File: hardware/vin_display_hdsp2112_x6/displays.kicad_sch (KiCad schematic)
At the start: 13 parts

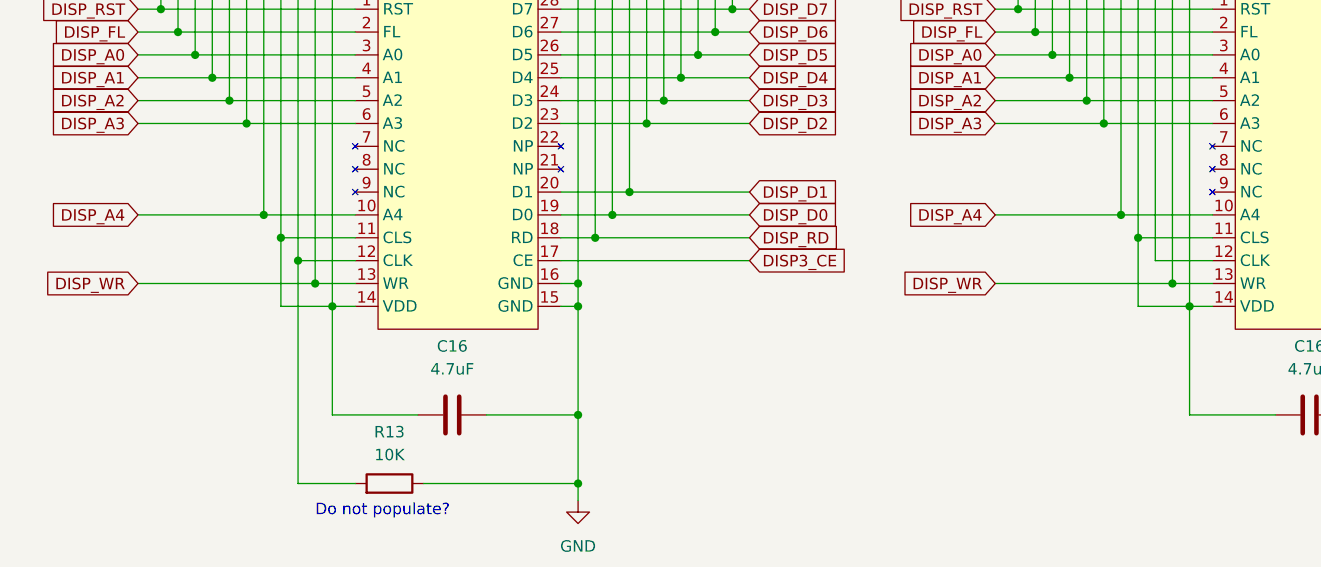
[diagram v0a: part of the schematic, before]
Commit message: work on hdsp2112_x6 pcb
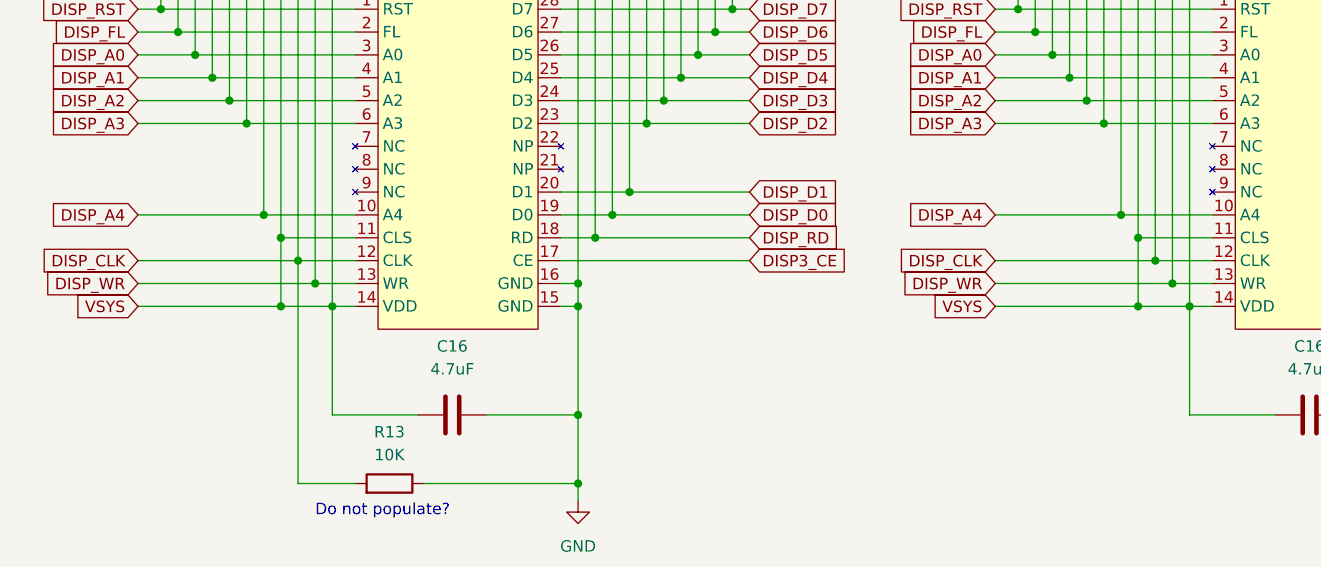
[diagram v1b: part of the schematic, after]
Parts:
- C16: footprint Capacitor_SMD:C_0603_1608Metric -> Capacitor_SMD:C_0805_2012Metric
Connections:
- net VSYS: now reaches C16.1, C16.1, C16.1, U10.11 (CLS), U10.14 (VDD), U8.11 (CLS), U8.14 (VDD), U9.11 (CLS), U9.14 (VDD)
- net VSYS: now also C16.1, C16.1, C16.1, U5.11 (CLS), U5.14 (VDD), U6.11 (CLS), U6.14 (VDD), U7.11 (CLS), U7.14 (VDD)
- net DISP_CLK: now reaches U10.12 (CLK), U8.12 (CLK), U9.12 (CLK)
- net DISP_CLK: now also R13.2, U5.12 (CLK), U6.12 (CLK), U7.12 (CLK)
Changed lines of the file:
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@@
   (junction (at 50.8 66.04) (diameter 0) (color 0 0 0 0)
   )
+  (junction (at 142.24 160.02) (diameter 0) (color 0 0 0 0)
+  )
   (junction (at 138.43 154.94) (diameter 0) (color 0 0 0 0)
   )
@@
   (junction (at 132.715 83.82) (diameter 0) (color 0 0 0 0)
   )
+  (junction (at 45.085 165.1) (diameter 0) (color 0 0 0 0)
+  )
   (junction (at 31.75 76.2) (diameter 0) (color 0 0 0 0)
   )
@@
   (junction (at 80.01 157.48) (diameter 0) (color 0 0 0 0)
   )
+  (junction (at 140.335 165.1) (diameter 0) (color 0 0 0 0)
+  )
   (junction (at 146.05 165.1) (diameter 0) (color 0 0 0 0)
   )
@@
     (stroke (width 0) (type default))
   )
+  (wire (pts (xy 29.21 160.02) (xy 46.99 160.02))
+    (stroke (width 0) (type default))
+  )
   (wire (pts (xy 128.905 78.74) (xy 148.59 78.74))
     (stroke (width 0) (type default))
@@
     (stroke (width 0) (type default))
   )
+  (wire (pts (xy 29.21 165.1) (xy 45.085 165.1))
+    (stroke (width 0) (type default))
+  )
   (wire (pts (xy 171.45 21.59) (xy 190.5 21.59))
     (stroke (width 0) (type default))
@@
     (stroke (width 0) (type default))
   )
+  (wire (pts (xy 124.46 165.1) (xy 140.335 165.1))
+    (stroke (width 0) (type default))
+  )
   (wire (pts (xy 85.725 144.78) (xy 76.2 144.78))
     (stroke (width 0) (type default))
@@
   )
   (wire (pts (xy 179.07 152.4) (xy 171.45 152.4))
+    (stroke (width 0) (type default))
+  )
+  (wire (pts (xy 124.46 160.02) (xy 142.24 160.02))
     (stroke (width 0) (type default))
   )
@@
     )
   )
+  (global_label "DISP_CLK" (shape input) (at 29.21 160.02 180) (fields_autoplaced)
+    (effects (font (size 1.27 1.27)) (justify right))
+    (property "Intersheetrefs" "${INTERSHEET_REFS}" (at 17.3348 160.02 0)
+      (effects (font (size 1.27 1.27)) (justify right) hide)
+    )
+  )
   (global_label "DISP_A4" (shape input) (at 124.46 154.94 180) (fields_autoplaced)
     (effects (font (size 1.27 1.27)) (justify right))
@@
     )
   )
+  (global_label "VSYS" (shape input) (at 124.46 165.1 180) (fields_autoplaced)
+    (effects (font (size 1.27 1.27)) (justify right))
+    (property "Intersheetrefs" "${INTERSHEET_REFS}" (at 116.8786 165.1 0)
+      (effects (font (size 1.27 1.27)) (justify right) hide)
+    )
+  )
   (global_label "DISP_D0" (shape input) (at 192.405 154.94 0) (fields_autoplaced)
     (effects (font (size 1.27 1.27)) (justify left))
@@
     )
   )
+  (global_label "DISP_CLK" (shape input) (at 124.46 160.02 180) (fields_autoplaced)
+    (effects (font (size 1.27 1.27)) (justify right))
+    (property "Intersheetrefs" "${INTERSHEET_REFS}" (at 112.5848 160.02 0)
+      (effects (font (size 1.27 1.27)) (justify right) hide)
+    )
+  )
   (global_label "DISP_D2" (shape input) (at 97.155 144.78 0) (fields_autoplaced)
     (effects (font (size 1.27 1.27)) (justify left))
@@
     (property "Intersheetrefs" "${INTERSHEET_REFS}" (at 109.0906 104.14 0)
       (effects (font (size 1.27 1.27)) (justify left) hide)
+    )
+  )
+  (global_label "VSYS" (shape input) (at 29.21 165.1 180) (fields_autoplaced)
+    (effects (font (size 1.27 1.27)) (justify right))
+    (property "Intersheetrefs" "${INTERSHEET_REFS}" (at 21.6286 165.1 0)
+      (effects (font (size 1.27 1.27)) (justify right) hide)
     )
   )
@@
       (effects (font (size 1.27 1.27)))
     )
-    (property "Footprint" "Capacitor_SMD:C_0603_1608Metric" (at 68.58 119.6848 0)
+    (property "Footprint" "Capacitor_SMD:C_0805_2012Metric" (at 68.58 119.6848 0)
       (effects (font (size 1.27 1.27)) hide)
     )
@@
       (effects (font (size 1.27 1.27)))
     )
-    (property "Footprint" "Capacitor_SMD:C_0603_1608Metric" (at 163.195 176.1998 0)
+    (property "Footprint" "Capacitor_SMD:C_0805_2012Metric" (at 163.195 176.1998 0)
       (effects (font (size 1.27 1.27)) hide)
     )
@@
       (effects (font (size 1.27 1.27)))
     )
-    (property "Footprint" "Capacitor_SMD:C_0603_1608Metric" (at 67.945 65.0748 0)
+    (property "Footprint" "Capacitor_SMD:C_0805_2012Metric" (at 67.945 65.0748 0)
       (effects (font (size 1.27 1.27)) hide)
     )
@@
       (effects (font (size 1.27 1.27)))
     )
-    (property "Footprint" "Capacitor_SMD:C_0603_1608Metric" (at 163.83 119.6848 0)
+    (property "Footprint" "Capacitor_SMD:C_0805_2012Metric" (at 163.83 119.6848 0)
       (effects (font (size 1.27 1.27)) hide)
     )
@@
       (effects (font (size 1.27 1.27)))
     )
-    (property "Footprint" "Capacitor_SMD:C_0603_1608Metric" (at 67.945 176.1998 0)
+    (property "Footprint" "Capacitor_SMD:C_0805_2012Metric" (at 67.945 176.1998 0)
       (effects (font (size 1.27 1.27)) hide)
     )
@@
       (effects (font (size 1.27 1.27)))
     )
-    (property "Footprint" "Capacitor_SMD:C_0603_1608Metric" (at 163.195 65.0748 0)
-      (effects (font (size 1.27 1.27)) hide)
-    )
+    (property "Footprint" "Capacitor_SMD:C_0805_2012Metric" (at 163.195 65.0748 0)
+      (effects (font (size 1.27 1.27)) hide)
+    )
